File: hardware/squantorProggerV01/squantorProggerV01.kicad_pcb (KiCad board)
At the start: 2 copper layers, 29 x 29 mm, 8 parts, among them J1 USB-ID, J2 JTAG_2X05_IN, J3 JTAG_2X05_OUT

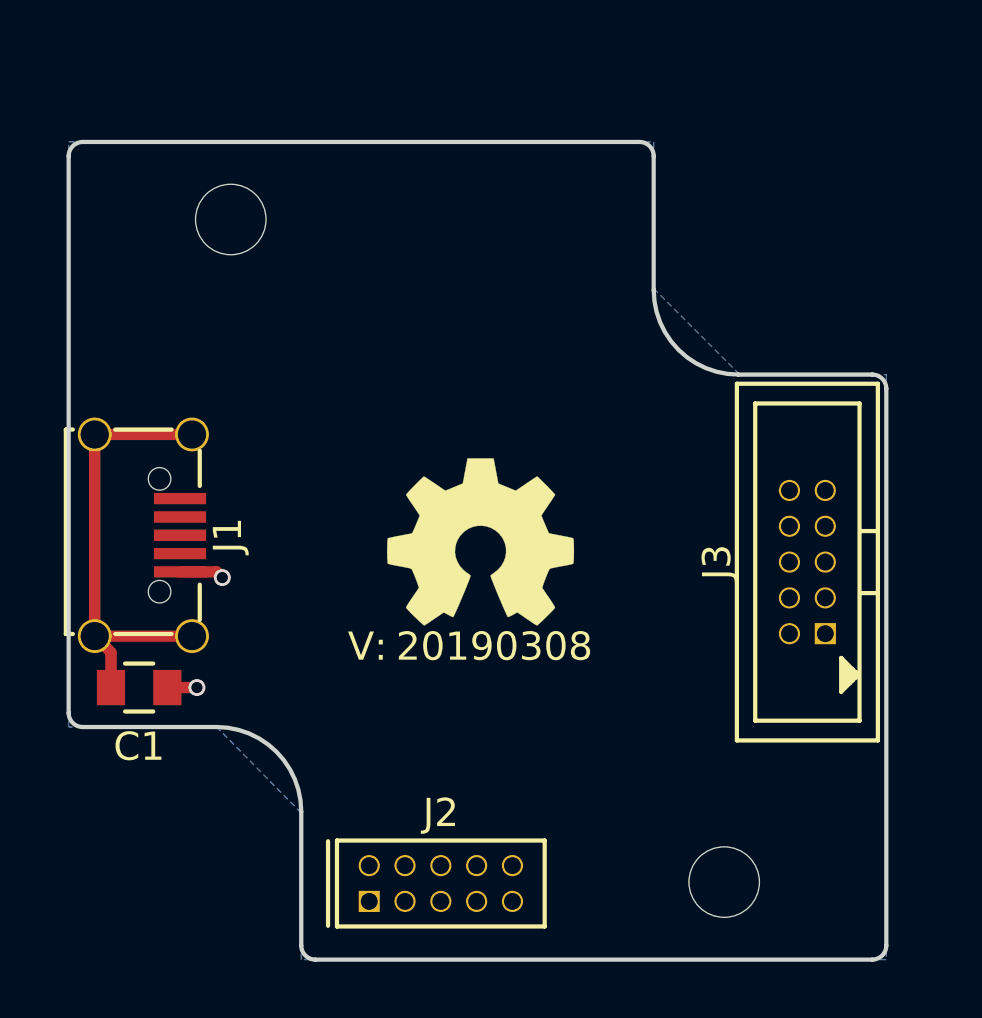
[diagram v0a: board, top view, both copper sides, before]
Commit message: imported schematics of LPC824 breakout and HT42B534 breakout
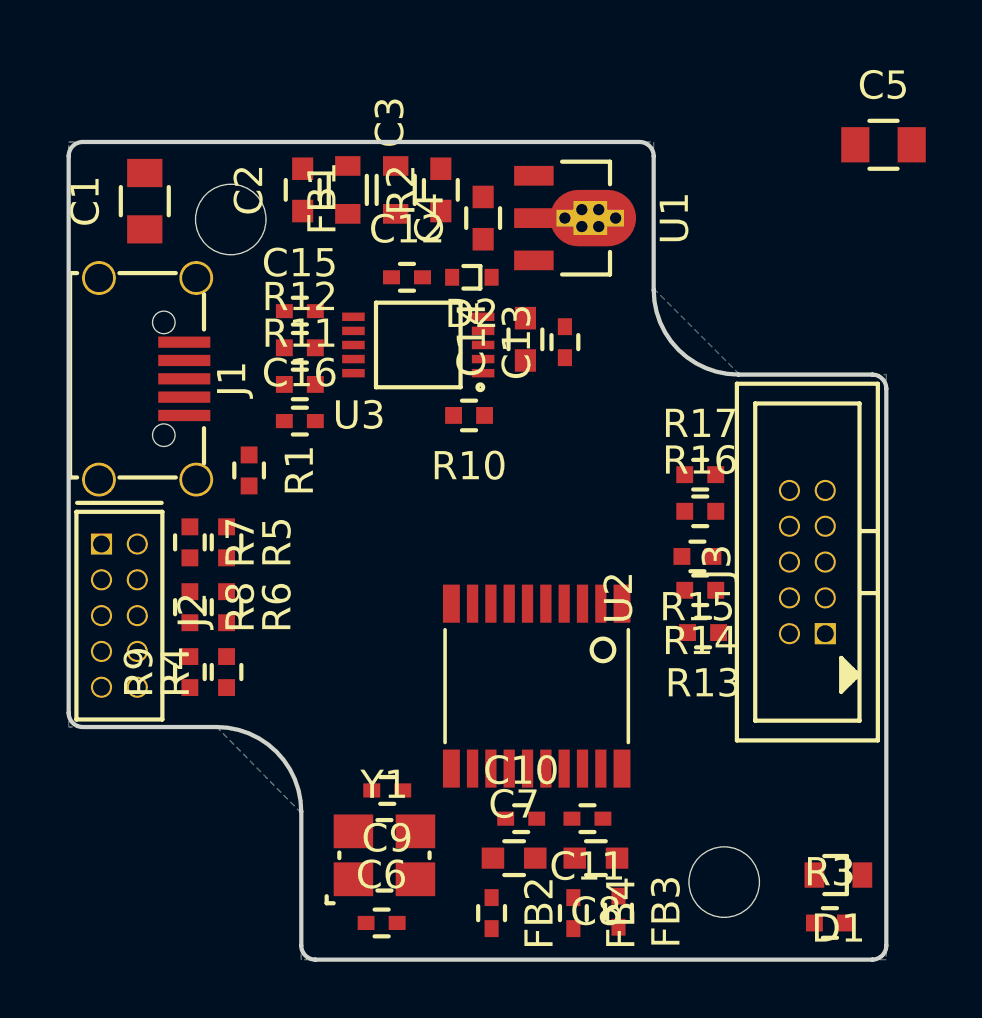
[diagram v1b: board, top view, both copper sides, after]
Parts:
- added C10: 100n, SquantorRcl:C_0402, F.Cu at (149.4, 110.8)
- added C11: 100n, SquantorRcl:C_0402, F.Cu at (151.8, 110.8)
- added C12: 100n, SquantorRcl:C_0402, F.Cu at (145.4, 91.6)
- added C13: 100n, SquantorRcl:C_0402, F.Cu at (151.0, 93.9)
- added C14: 1u, SquantorRcl:C_0603, F.Cu at (149.6, 93.8)
- added C15: 47p, SquantorRcl:C_0402, F.Cu at (141.6, 92.8)
- added C16: 47p, SquantorRcl:C_0402, F.Cu at (141.6, 96.7)
- added C2: 100n, SquantorRcl:C_0603, F.Cu at (141.7, 88.5)
- added C3: 1u, SquantorRcl:C_0603, F.Cu at (146.6, 88.5)
- added C4: 1u, SquantorRcl:C_0603, F.Cu at (148.1, 89.5)
- added C5: 10u, SquantorRcl:C_0805, F.Cu at (162.3, 86.9)
- added C6: 18p, SquantorRcl:C_0402, F.Cu at (144.5, 114.5)
- added C7: 1u, SquantorRcl:C_0603, F.Cu at (149.2, 112.2)
- added C8: 1u, SquantorRcl:C_0603, F.Cu at (152.1, 112.2)
- added C9: 18p, SquantorRcl:C_0402, F.Cu at (144.7, 109.8)
- added D1: RED, SquantorDiodes:D_0603_hand, F.Cu at (160.7, 112.8)
- added D2: D, SquantorDiodes:SOD-523, F.Cu at (147.7, 91.6)
- added FB1: 600, SquantorRcl:R_0603_hand, F.Cu at (145.0, 88.5)
- added FB2: FB, SquantorRcl:C_0402, F.Cu at (148.4, 114.2)
- added FB3: FB, SquantorRcl:C_0402, F.Cu at (152.9, 114.1)
- added FB4: FB, SquantorRcl:C_0402, F.Cu at (151.3, 114.2)
- added R1: 0, SquantorRcl:R_0402_hand, F.Cu at (139.8, 98.5)
- added R10: 10K, SquantorRcl:R_0402_hand, F.Cu at (147.6, 96.5)
- added R11: 33, SquantorRcl:R_0402_hand, F.Cu at (141.6, 95.4)
- added R12: 33, SquantorRcl:R_0402_hand, F.Cu at (141.6, 94.1)
- added R13: 100, SquantorRcl:R_0402_hand, F.Cu at (155.9, 104.2)
- added R14: 100, SquantorRcl:R_0402_hand, F.Cu at (155.8, 102.7)
- added R15: 100, SquantorRcl:R_0402_hand, F.Cu at (155.7, 101.5)
- added R16: 100, SquantorRcl:R_0402_hand, F.Cu at (155.8, 99.9)
- added R17: 100, SquantorRcl:R_0402_hand, F.Cu at (155.8, 98.6)
- added R2: Fuse, SquantorRcl:R_0603_hand, F.Cu at (143.3, 88.5)
- added R3: 1K, SquantorRcl:R_0402_hand, F.Cu at (160.4, 114.5)
- added R4: 100K, SquantorRcl:R_0402_hand, F.Cu at (139.0, 105.6)
- added R5: 100k, SquantorRcl:R_0402_hand, F.Cu at (139.0, 101.0)
- added R6: 100k, SquantorRcl:R_0402_hand, F.Cu at (139.0, 103.3)
- added R7: 100, SquantorRcl:R_0402_hand, F.Cu at (137.7, 101.0)
- added R8: 100, SquantorRcl:R_0402_hand, F.Cu at (137.7, 103.3)
- added R9: 100, SquantorRcl:R_0402_hand, F.Cu at (137.7, 105.6)
- added U1: MCP1702-MB, SquantorIC:SOT89-ViaTab-Microchip-MB, F.Cu at (149.9, 89.5)
- added U2: LPC824M201JDH20, SquantorIC:SOT360, F.Cu at (150.0, 106.1)
- added U3: HT42B534-MSOP10, SquantorIC:MSOP-10, F.Cu at (145.8, 94.0)
- added Y1: 12MHz, SquantorCrystal:Crystal_3225_4, F.Cu at (144.6, 112.1)
- J2: value JTAG_2X05_IN -> JTAG_2X05
- N1: footprint Symbols:OSHW-Symbol_6.7x6mm_SilkScreen -> Symbol:OSHW-Symbol_6.7x6mm_SilkScreen; moved to B.Cu
- N2: value 20190308 -> 20190402; moved to B.Cu
- moved N1 30.6 mm to (173.0, 118.7)
- moved N2 24.8 mm to (171.6, 114.9)
- moved C1 17.3 mm to (136.1, 88.9), turned to 90 degrees
- moved J2 14.8 mm to (135.2, 103.6), turned to 270 degrees
- moved J1 5.55 mm to (136.2, 95.2)
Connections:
- C1 pad 1: VSS -> Net-(C1-Pad1)
- C1 pad 2: Net-(C1-Pad2) -> VSS
- J1 pad 1: (no net) -> /VBUS
- J1 pad 2: (no net) -> /USB_D-
- J1 pad 3: (no net) -> /USB_D+
- J1 pad 4: (no net) -> Net-(J1-Pad4)
- J1 pad S: Net-(C1-Pad2) -> Net-(C1-Pad1)
- J2 pad 1: (no net) -> /VDD
- J2 pad 10: (no net) -> Net-(J2-Pad10)
- J2 pad 2: (no net) -> Net-(J2-Pad2)
- J2 pad 4: (no net) -> Net-(J2-Pad4)
- J3 pad 10: (no net) -> Net-(J3-Pad10)
- J3 pad 2: (no net) -> Net-(J3-Pad2)
- J3 pad 4: (no net) -> Net-(J3-Pad4)
- J3 pad 6: (no net) -> Net-(J3-Pad6)
- J3 pad 8: (no net) -> Net-(J3-Pad8)
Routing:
- net Net-(C1-Pad2): track 16.1 -> 0.00 mm
- net VSS: track 2.63 -> 0.00 mm, vias 2 -> 0

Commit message: added test points to USB and SWD in
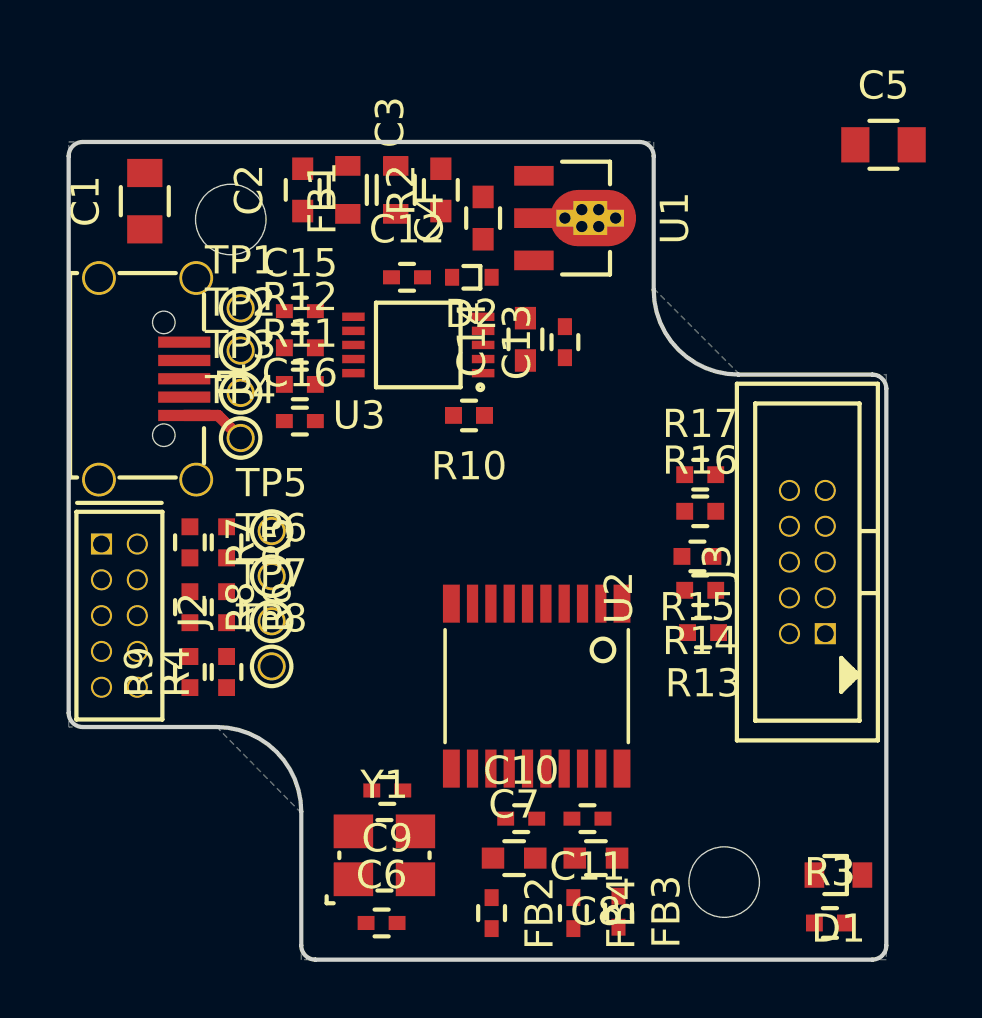
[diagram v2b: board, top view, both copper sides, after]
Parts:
- removed R1: 0, SquantorRcl:R_0402_hand
- added TP1: testpad, SquantorTestPoints:TestPoint_Hole_D0.8mm, F.Cu at (139.5, 92.7)
- added TP2: testpad, SquantorTestPoints:TestPoint_Hole_D0.8mm, F.Cu at (139.5, 94.2)
- added TP3: testpad, SquantorTestPoints:TestPoint_Hole_D0.8mm, F.Cu at (139.5, 95.7)
- added TP4: testpad, SquantorTestPoints:TestPoint_Hole_D0.8mm, F.Cu at (139.5, 97.3)
- added TP5: testpad, SquantorTestPoints:TestPoint_Hole_D0.8mm, F.Cu at (140.6, 100.6)
- added TP6: testpad, SquantorTestPoints:TestPoint_Hole_D0.8mm, F.Cu at (140.6, 102.2)
- added TP7: testpad, SquantorTestPoints:TestPoint_Hole_D0.8mm, F.Cu at (140.6, 103.8)
- added TP8: testpad, SquantorTestPoints:TestPoint_Hole_D0.8mm, F.Cu at (140.6, 105.4)
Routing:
- net VSS: track 0.00 -> 2.33 mm
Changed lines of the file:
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@@
     (thickness 1.6)
     (drawings 16)
-    (tracks 0)
+    (tracks 2)
     (zones 0)
-    (modules 50)
+    (modules 57)
     (nets 31)
   )
@@
   )
   (setup
-    (last_trace_width 0.1524)
+    (last_trace_width 0.4)
     (user_trace_width 0.1524)
     (user_trace_width 0.2)
@@
     (add_net VSS)
   )
+  (module SquantorTestPoints:TestPoint_Hole_D0.8mm (layer F.Cu)
+    (at 140.6 105.4)
+    (fp_text reference TP8 (at 0 -1.7) (layer F.SilkS)
+      (effects (font (size 1 1) (thickness 0.15)))
+    )
+    (fp_text value testpad (at 0 1.9) (layer F.Fab)
+      (effects (font (size 1 1) (thickness 0.15)))
+    )
+    (fp_circle (center 0 0) (end 0.7 0) (layer F.SilkS) (width 0.15))
+    (pad 1 thru_hole circle (at 0 0) (size 1 1) (drill 0.8) (layers *.Cu *.Mask)
+      (net 1 VSS))
+  )
+  (module SquantorTestPoints:TestPoint_Hole_D0.8mm (layer F.Cu)
+    (at 140.6 103.8)
+    (fp_text reference TP7 (at 0 -1.7) (layer F.SilkS)
+      (effects (font (size 1 1) (thickness 0.15)))
+    )
+    (fp_text value testpad (at 0 1.9) (layer F.Fab)
+      (effects (font (size 1 1) (thickness 0.15)))
+    )
+    (fp_circle (center 0 0) (end 0.7 0) (layer F.SilkS) (width 0.15))
+    (pad 1 thru_hole circle (at 0 0) (size 1 1) (drill 0.8) (layers *.Cu *.Mask)
+      (net 25 /RESET))
+  )
+  (module SquantorTestPoints:TestPoint_Hole_D0.8mm (layer F.Cu)
+    (at 140.6 102.2)
+    (fp_text reference TP6 (at 0 -1.7) (layer F.SilkS)
+      (effects (font (size 1 1) (thickness 0.15)))
+    )
+    (fp_text value testpad (at 0 1.9) (layer F.Fab)
+      (effects (font (size 1 1) (thickness 0.15)))
+    )
+    (fp_circle (center 0 0) (end 0.7 0) (layer F.SilkS) (width 0.15))
+    (pad 1 thru_hole circle (at 0 0) (size 1 1) (drill 0.8) (layers *.Cu *.Mask)
+      (net 27 /PIO0_3))
+  )
+  (module SquantorTestPoints:TestPoint_Hole_D0.8mm (layer F.Cu)
+    (at 140.6 100.6)
+    (fp_text reference TP5 (at 0 -1.7) (layer F.SilkS)
+      (effects (font (size 1 1) (thickness 0.15)))
+    )
+    (fp_text value testpad (at 0 1.9) (layer F.Fab)
+      (effects (font (size 1 1) (thickness 0.15)))
+    )
+    (fp_circle (center 0 0) (end 0.7 0) (layer F.SilkS) (width 0.15))
+    (pad 1 thru_hole circle (at 0 0) (size 1 1) (drill 0.8) (layers *.Cu *.Mask)
+      (net 26 /PIO0_2))
+  )
+  (module SquantorTestPoints:TestPoint_Hole_D0.8mm (layer F.Cu)
+    (at 139.5 97.3)
+    (fp_text reference TP4 (at 0 -1.7) (layer F.SilkS)
+      (effects (font (size 1 1) (thickness 0.15)))
+    )
+    (fp_text value testpad (at 0 1.9) (layer F.Fab)
+      (effects (font (size 1 1) (thickness 0.15)))
+    )
+    (fp_circle (center 0 0) (end 0.7 0) (layer F.SilkS) (width 0.15))
+    (pad 1 thru_hole circle (at 0 0) (size 1 1) (drill 0.8) (layers *.Cu *.Mask)
+      (net 1 VSS))
+  )
+  (module SquantorTestPoints:TestPoint_Hole_D0.8mm (layer F.Cu)
+    (at 139.5 95.7)
+    (fp_text reference TP3 (at 0 -1.7) (layer F.SilkS)
+      (effects (font (size 1 1) (thickness 0.15)))
+    )
+    (fp_text value testpad (at 0 1.9) (layer F.Fab)
+      (effects (font (size 1 1) (thickness 0.15)))
+    )
+    (fp_circle (center 0 0) (end 0.7 0) (layer F.SilkS) (width 0.15))
+    (pad 1 thru_hole circle (at 0 0) (size 1 1) (drill 0.8) (layers *.Cu *.Mask)
+      (net 30 /USB_D+))
+  )
+  (module SquantorTestPoints:TestPoint_Hole_D0.8mm (layer F.Cu)
+    (at 139.5 94.2)
+    (fp_text reference TP2 (at 0 -1.7) (layer F.SilkS)
+      (effects (font (size 1 1) (thickness 0.15)))
+    )
+    (fp_text value testpad (at 0 1.9) (layer F.Fab)
+      (effects (font (size 1 1) (thickness 0.15)))
+    )
+    (fp_circle (center 0 0) (end 0.7 0) (layer F.SilkS) (width 0.15))
+    (pad 1 thru_hole circle (at 0 0) (size 1 1) (drill 0.8) (layers *.Cu *.Mask)
+      (net 29 /USB_D-))
+  )
+  (module SquantorTestPoints:TestPoint_Hole_D0.8mm (layer F.Cu)
+    (at 139.5 92.7)
+    (fp_text reference TP1 (at 0 -1.7) (layer F.SilkS)
+      (effects (font (size 1 1) (thickness 0.15)))
+    )
+    (fp_text value testpad (at 0 1.9) (layer F.Fab)
+      (effects (font (size 1 1) (thickness 0.15)))
+    )
+    (fp_circle (center 0 0) (end 0.7 0) (layer F.SilkS) (width 0.15))
+    (pad 1 thru_hole circle (at 0 0) (size 1 1) (drill 0.8) (layers *.Cu *.Mask)
+      (net 3 /VBUS))
+  )
   (module SquantorRcl:C_0603 (layer F.Cu)
     (at 141.7 88.5 90)
@@
       (net 15 "Net-(FB1-Pad2)"))
     (model Resistors_SMD.3dshapes/R_0603.wrl
-      (at (xyz 0 0 0))
-      (scale (xyz 1 1 1))
-      (rotate (xyz 0 0 0))
-    )
-  )
-  (module SquantorRcl:R_0402_hand (layer F.Cu)
-    (at 139.8 98.45 270)
-    (descr "Resistor SMD 0402, reflow soldering, Vishay (see dcrcw.pdf)")
-    (tags "resistor 0402")
-    (attr smd)
-    (fp_text reference R1 (at 0 -1.8 270) (layer F.SilkS)
-      (effects (font (size 1 1) (thickness 0.15)))
-    )
-    (fp_text value 0 (at 0 1.8 270) (layer F.Fab)
-      (effects (font (size 1 1) (thickness 0.15)))
-    )
-    (fp_line (start -0.25 0.525) (end 0.25 0.525) (layer F.SilkS) (width 0.15))
-    (fp_line (start 0.25 -0.525) (end -0.25 -0.525) (layer F.SilkS) (width 0.15))
-    (fp_line (start 1.15 -0.65) (end 1.15 0.65) (layer F.CrtYd) (width 0.05))
-    (fp_line (start -1.15 -0.65) (end -1.15 0.65) (layer F.CrtYd) (width 0.05))
-    (fp_line (start -1.15 0.65) (end 1.15 0.65) (layer F.CrtYd) (width 0.05))
-    (fp_line (start -1.15 -0.65) (end 1.15 -0.65) (layer F.CrtYd) (width 0.05))
-    (fp_line (start -0.5 -0.25) (end 0.5 -0.25) (layer F.Fab) (width 0.1))
-    (fp_line (start 0.5 -0.25) (end 0.5 0.25) (layer F.Fab) (width 0.1))
-    (fp_line (start 0.5 0.25) (end -0.5 0.25) (layer F.Fab) (width 0.1))
-    (fp_line (start -0.5 0.25) (end -0.5 -0.25) (layer F.Fab) (width 0.1))
-    (pad 2 smd rect (at 0.55 0 270) (size 0.6 0.6) (layers F.Cu F.Paste F.Mask)
-      (net 1 VSS))
-    (pad 1 smd rect (at -0.55 0 270) (size 0.6 0.6) (layers F.Cu F.Paste F.Mask)
-      (net 16 "Net-(J1-Pad4)"))
-    (model Resistors_SMD.3dshapes/R_0402.wrl
       (at (xyz 0 0 0))
       (scale (xyz 1 1 1))
@@
   (gr_arc (start 153.65 87.3) (end 154.15 87.3) (angle -90) (layer Edge.Cuts) (width 0.15))
   (gr_line (start 133.9 86.8) (end 153.65 86.8) (layer Edge.Cuts) (width 0.15))
+  (segment (start 138.7 96.5) (end 139.5 97.3) (width 0.4) (layer F.Cu) (net 1))
+  (segment (start 137.5 96.5) (end 138.7 96.5) (width 0.4) (layer F.Cu) (net 1))
   (zone (net 1) (net_name VSS) (layer B.Cu) (hatch edge 0.508)
     (connect_pads (clearance 0.3))

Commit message: updated footprint
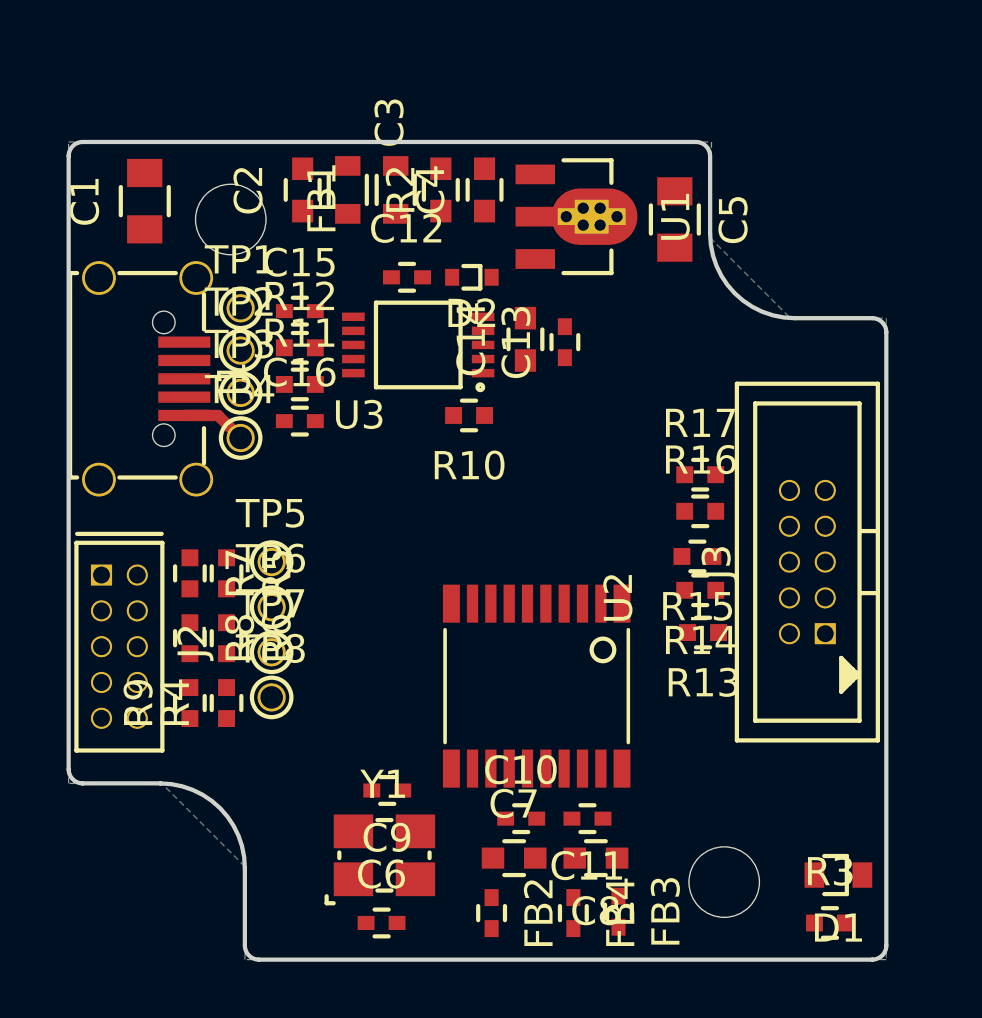
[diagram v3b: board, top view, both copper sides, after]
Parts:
- N2: value 20190402 -> 20190520
- moved C5 7.86 mm to (154.9, 89.5), turned to 270 degrees
- moved J2 1.10 mm to (135.2, 104.7)
- moved R4 1.10 mm to (139.0, 106.7)
- moved R6 1.10 mm to (139.0, 104.4)
- moved R8 1.10 mm to (137.7, 104.4)
- moved R9 1.10 mm to (137.7, 106.7)
- moved TP5 1.10 mm to (140.6, 101.7)
- moved TP7 1.10 mm to (140.6, 104.9)
- moved R5 1.10 mm to (139.0, 102.1)
- moved R7 1.10 mm to (137.7, 102.1)
- moved TP6 1.10 mm to (140.6, 103.3)
- moved TP8 1.10 mm to (140.6, 106.5)
- moved C4 1.00 mm to (148.2, 88.5)
- moved U1 0.07 mm to (149.9, 89.5)
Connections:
- J1 pad 4: Net-(J1-Pad4) -> (no net)
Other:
- outline, holes or cut-outs redrawn
